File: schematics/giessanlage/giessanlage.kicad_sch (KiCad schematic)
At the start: 17 parts, among them P1 Pumpe, P2 Pumpe, Q1 IRLZ34N, Q2 IRLZ34N, SW1 P1_Manuell_On, SW2 P1_Manuell_On, SW3 Manuell_Off, U1 ESP32-C6-DevKitC-1

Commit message: feat: schematics and doc update
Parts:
- added Chirp: (no value), symbol 01_own:Chirp
- added Q3: NX2301P, Package_TO_SOT_SMD:SOT-23, symbol Transistor_FET:IRLML6402
- added R5, R6: 4.7k, symbol CERN:Resistor
- added R7: 100, symbol CERN:Resistor
- added R8: 10k, symbol CERN:Resistor
- added Ultraschall: (no value), symbol 01_own:Ultraschall
- added tof: (no value), symbol 01_own:Tof
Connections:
- net at SW1.1, SW2.1, SW3.1: now also U1.15 (GND); no longer U1.32 (GND)
- net at U1.1 (3V3): now also Chirp.1 (VCC), Q3.2 (S), R5.1, R6.1, R8.2, Ultraschall.3 (RX), tof.1 (VIN)
- net at U1.25 (GPIO20): now also tof.6 (SHUT)
- net at U1.30 (GPIO17/U0RXD): now also Ultraschall.4 (TX)
- net at U1.31 (GPIO16/U0TXD): now also R7.1
- net at U1.5 (GPIO6): now also Chirp.2 (SDA), R5.2, tof.3 (SDA)
- net at U1.6 (GPIO7): now also Chirp.3 (SCL), R6.2, tof.4 (SCL)
- new net: Q3.1 (G), R7.2, R8.1
- new net: Chirp.6 (GND), U1.32 (GND), Ultraschall.2 (GND), tof.2 (GND)
- new net: Q3.3 (D), Ultraschall.1 (VCC)
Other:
- moved on the sheet: BT1, D1, D2, P1, P2, Q1, Q2, R1, R2, R3, R4, SC1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

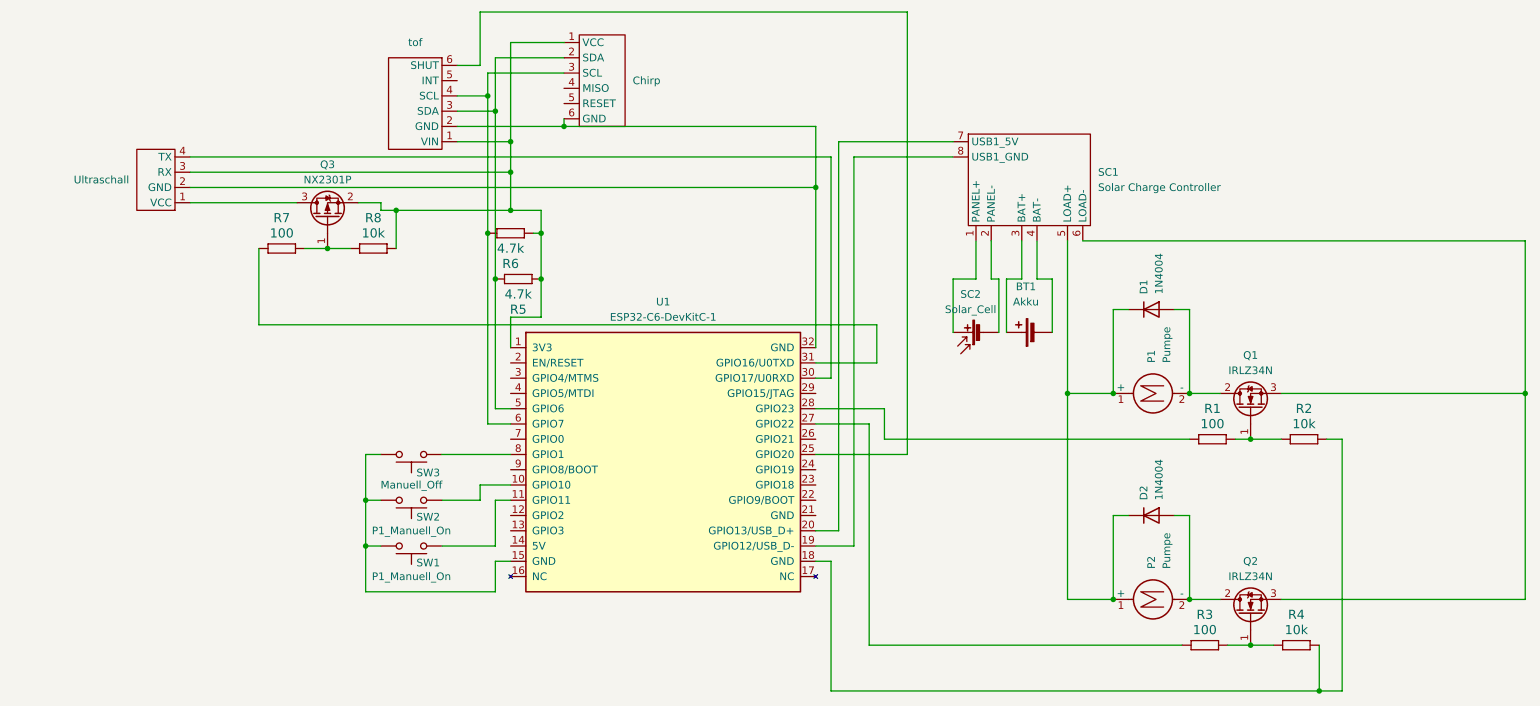
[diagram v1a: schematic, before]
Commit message: schematic: add e-paper, move pumps to GPIO22/23, buttons to GPIO10/11/1, TOF to GPIO0
Reflects in-place schematic edits making KiCad the authoritative source
of truth. Pumps and buttons swap from the old Nano-era layout, TOF
XSHUT relocates from GPIO20 to GPIO0 to free GPIO20 for the e-paper
CS line, and the 2.9" tri-colour e-paper (Reichelt #253924) lands on
GPIO18/19/20/21/3/2.
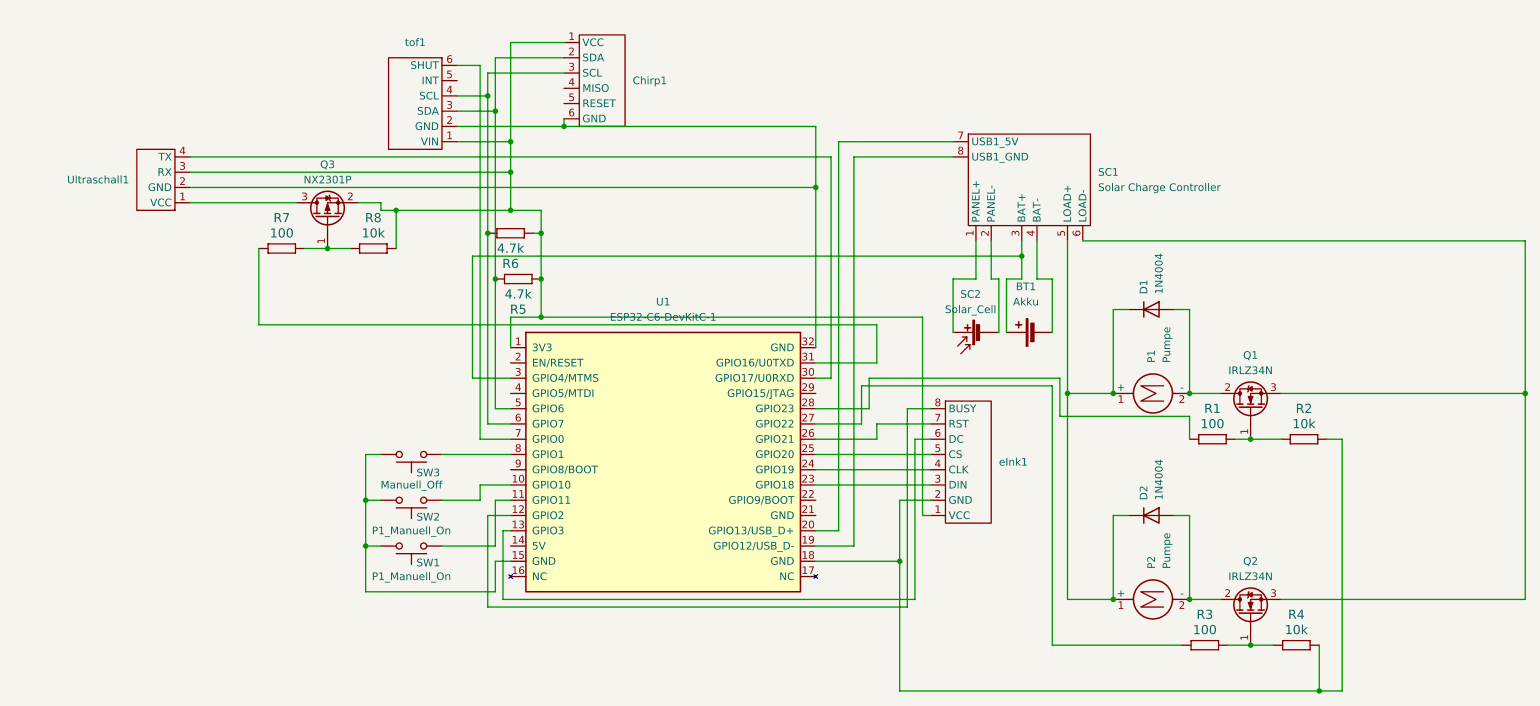
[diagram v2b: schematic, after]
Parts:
- added eInk1: (no value), symbol 01_own:eInk
- renumbered Chirp to Chirp1, Ultraschall to Ultraschall1, tof to tof1
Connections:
- net at Chirp1.1 (VCC), Q3.2 (S), R5.1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: now also eInk1.1 (VCC)
- net at R2.2, R4.2, U1.18 (GND): now also eInk1.2 (GND)
- net at BT1.1 (+), SC1.3 (BAT+): now also U1.3 (GPIO4/MTMS)
- net at U1.12 (GPIO2): now also eInk1.8 (BUSY)
- net at U1.13 (GPIO3): now also eInk1.6 (DC)
- net at U1.23 (GPIO18): now also eInk1.3 (DIN)
- net at U1.24 (GPIO19): now also eInk1.4 (CLK)
- net at U1.25 (GPIO20): now also eInk1.5 (CS); no longer tof1.6 (SHUT)
- net at U1.26 (GPIO21): now also eInk1.7 (RST)
- net at U1.7 (GPIO0): now also tof1.6 (SHUT)
